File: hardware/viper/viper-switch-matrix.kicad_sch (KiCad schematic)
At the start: 127 parts, among them SW1 SW_Push, SW10 SW_Push, SW11 SW_Push, SW12 SW_Push, SW13 SW_Push, SW14 SW_Push, SW14_1 SW_Push, SW15 SW_Push, SW16 SW_Push, SW17 SW_Push, SW18 SW_Push, SW19 SW_Push, SW2 SW_Push, SW20 SW_Push, SW21 SW_Push, SW22 SW_Push, SW23 SW_Push, SW24 SW_Push, SW25 SW_Push, SW26 SW_Push, SW27 SW_Push, SW28 SW_Push, SW29 SW_Push, SW3 SW_Push, SW30 SW_Push, SW30_1 SW_Push, SW31 SW_Push, SW32 SW_Push, SW33 SW_Push, SW34 SW_Push, SW35 SW_Push, SW36 SW_Push, SW37 SW_Push, SW38 SW_Push, SW39 SW_Push, SW4 SW_Push, SW40 SW_Push, SW41 SW_Push, SW42 SW_Push, SW43 SW_Push, SW44 SW_Push, SW45 SW_Push, SW46 SW_Push, SW47 SW_Push, SW48 SW_Push, SW49 SW_Push, SW5 SW_Push, SW50 SW_Push, SW51 SW_Push, SW52 SW_Push, SW53 SW_Push, SW54 SW_Push, SW54_1 SW_Push, SW55 SW_Push, SW56 SW_Push, SW57 SW_Push, SW58 SW_Push, SW59 SW_Push, SW6 SW_Push, SW60 SW_Push, SW61 SW_Push, SW62 SW_Push, SW7 SW_Push, SW8 SW_Push, SW9 SW_Push

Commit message: Improved schematic
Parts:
- D1, D10, D11, D12, D13, D14, D15, D16, D17, D18, D19, D2, D20, D21, D22, D23, D24, D25, D26, D27, D28, D29, D3, D30, D31, D32, D33, D34, D35, D36, D37, D38, D39, D4, D40, D41, D42, D43, D44, D45, D46, D47, D48, D49, D5, D50, D51, D52, D53, D54, D55, D56, D57, D58, D59, D6, D60, D61, D62, D7, D8, D9: footprint Diode_SMD:D_0805_2012Metric_Pad1.15x1.40mm_HandSolder -> Diode_SMD:D_0805_2012Metric

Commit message: Updated BOM
Start with manufacturing files.
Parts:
- D1, D10, D11, D12, D13, D14, D15, D16, D17, D18, D19, D2, D20, D21, D22, D23, D24, D25, D26, D27, D28, D29, D3, D30, D31, D32, D33, D34, D35, D36, D37, D38, D39, D4, D40, D41, D42, D43, D44, D45, D46, D47, D48, D49, D5, D50, D51, D52, D53, D54, D55, D56, D57, D58, D59, D6, D60, D61, D62, D7, D8, D9: LCSC (none) -> C109001
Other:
- title: (none) -> Psyduck Viper

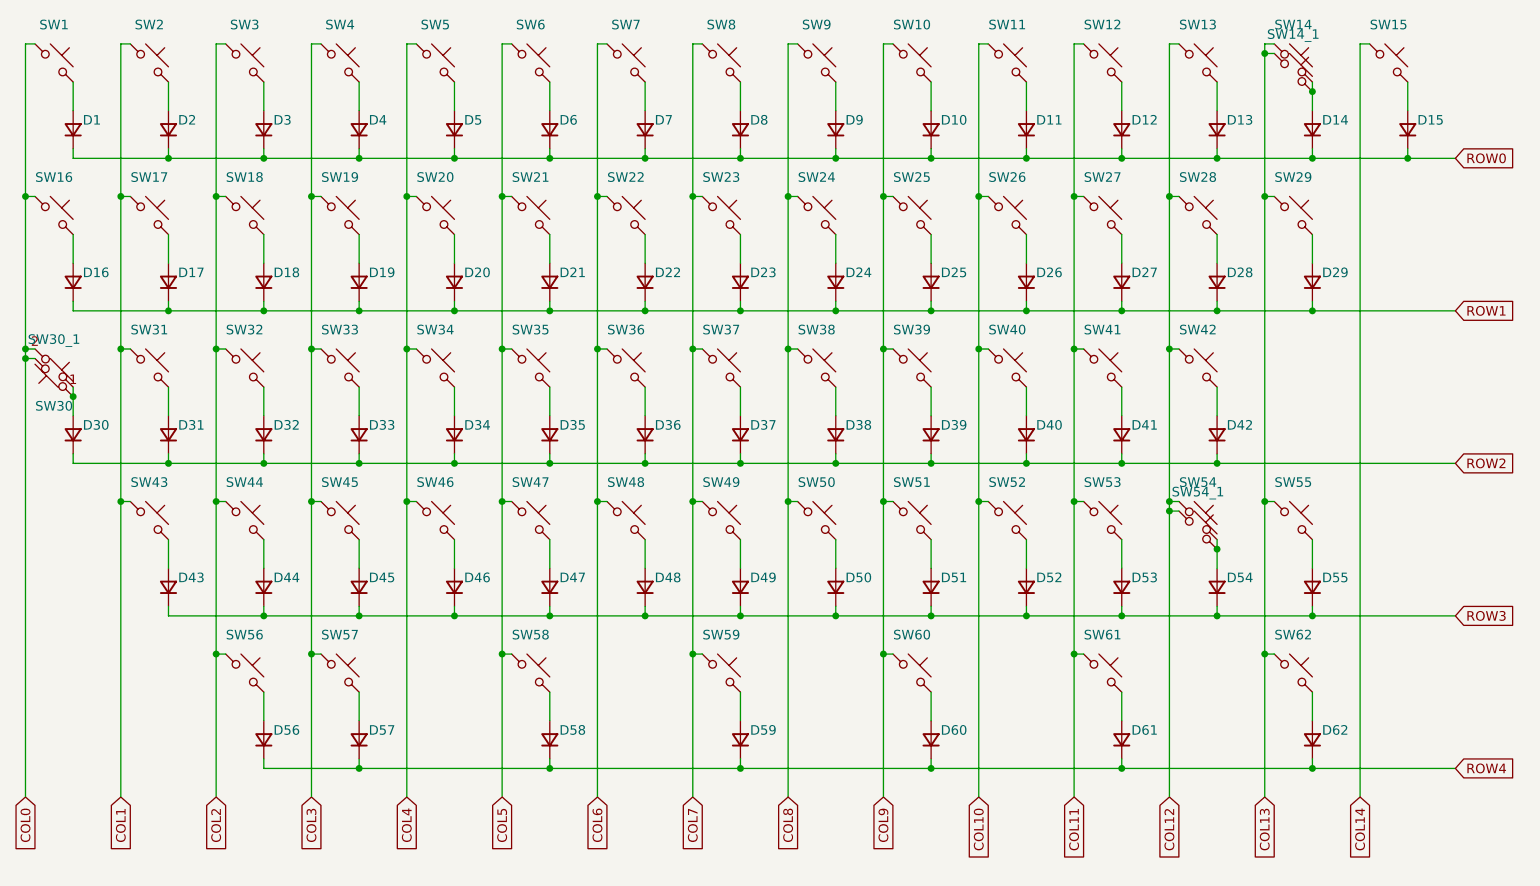
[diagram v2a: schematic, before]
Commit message: Debugging footprints for cleaner DRC
Set soldermask properties & improved ref placement on back silkscreen

Silkscreen ref placement & forked HRO type-c receptacle due to edge cut

Flipping switches
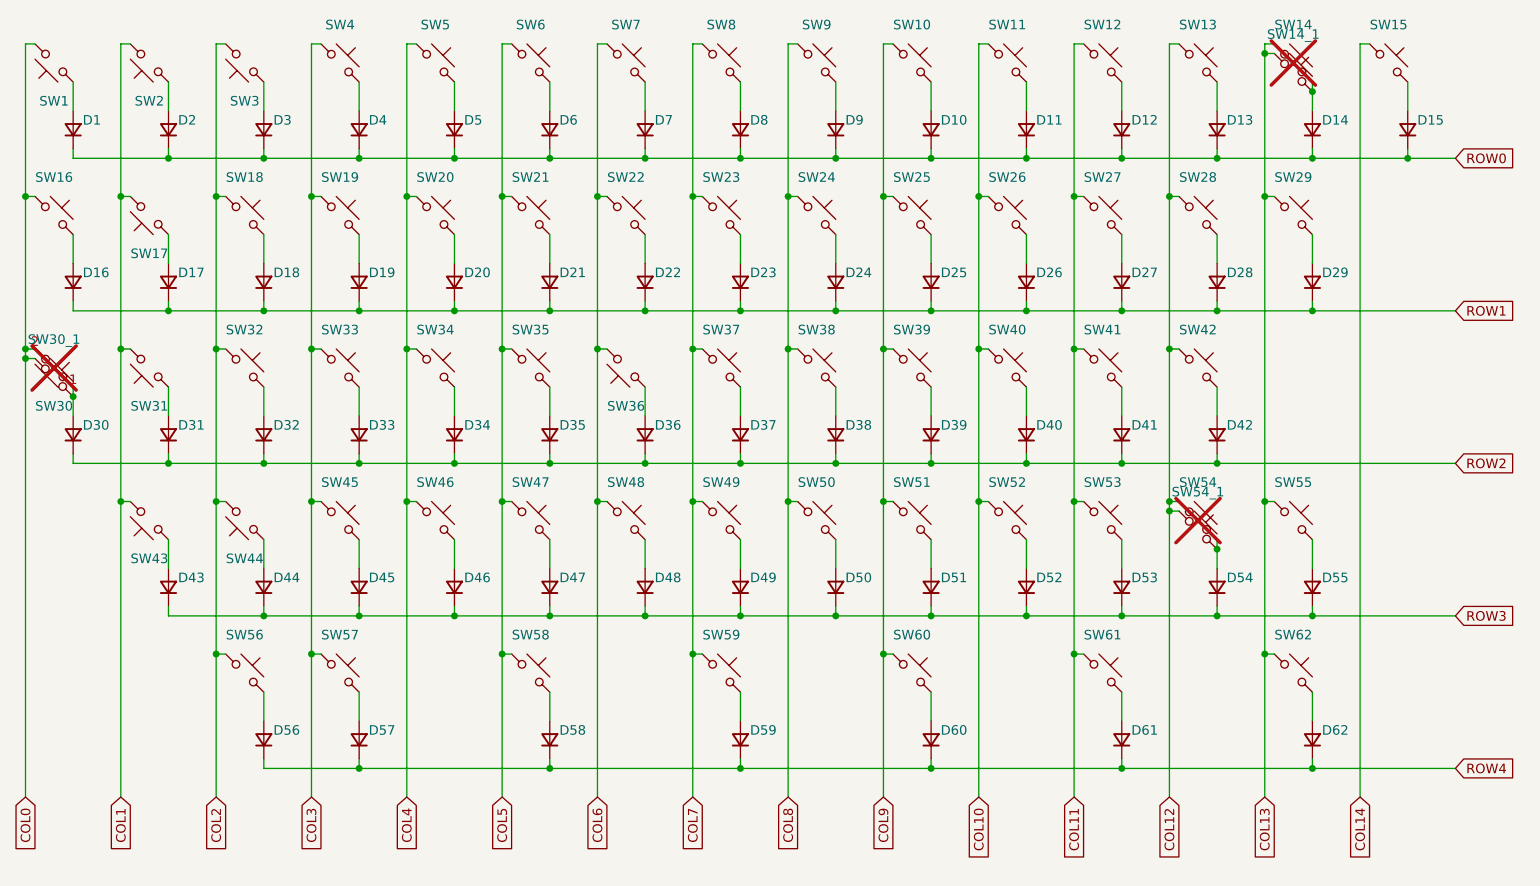
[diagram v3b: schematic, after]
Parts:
- SW1, SW10, SW11, SW12, SW13, SW14_1, SW15, SW16, SW17, SW18, SW19, SW2, SW20, SW21, SW22, SW23, SW24, SW25, SW26, SW27, SW28, SW29, SW3, SW30_1, SW31, SW32, SW33, SW34, SW35, SW36, SW37, SW38, SW39, SW4, SW40, SW41, SW42, SW43, SW44, SW45, SW46, SW47, SW48, SW49, SW5, SW50, SW51, SW52, SW53, SW54_1, SW55, SW56, SW57, SW58, SW59, SW6, SW60, SW61, SW62, SW7, SW8, SW9: footprint locallib:SW_Hybrid_Cherry_MX_Alps_1.00u -> locallib:SW_Hybrid_Cherry_MX_Alps_1.00u_1
- SW14, SW30, SW54: footprint locallib:SW_Hybrid_Cherry_MX_Alps_1.00u -> locallib:SW_Hybrid_Cherry_MX_Alps_1.00u_1; now not fitted
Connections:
- net COL0: now also SW1.2; no longer SW1.1
- net COL1: now also SW17.2, SW2.2, SW31.2, SW43.2; no longer SW17.1, SW2.1, SW31.1, SW43.1
- net COL2: now also SW3.2, SW44.2; no longer SW3.1, SW44.1
- net COL6: now also SW36.2; no longer SW36.1
- net at D2.2 (A): now also SW2.1; no longer SW2.2
- net at D31.2 (A): now also SW31.1; no longer SW31.2
- net at D1.2 (A): now also SW1.1; no longer SW1.2
- net at D3.2 (A): now also SW3.1; no longer SW3.2
- net at D44.2 (A): now also SW44.1; no longer SW44.2
- net at D17.2 (A): now also SW17.1; no longer SW17.2
- net at D43.2 (A): now also SW43.1; no longer SW43.2
- net at D36.2 (A): now also SW36.1; no longer SW36.2
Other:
- moved on the sheet: SW1, SW17, SW2, SW3, SW31, SW36, SW43, SW44
